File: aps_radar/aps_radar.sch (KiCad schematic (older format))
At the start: 0 parts

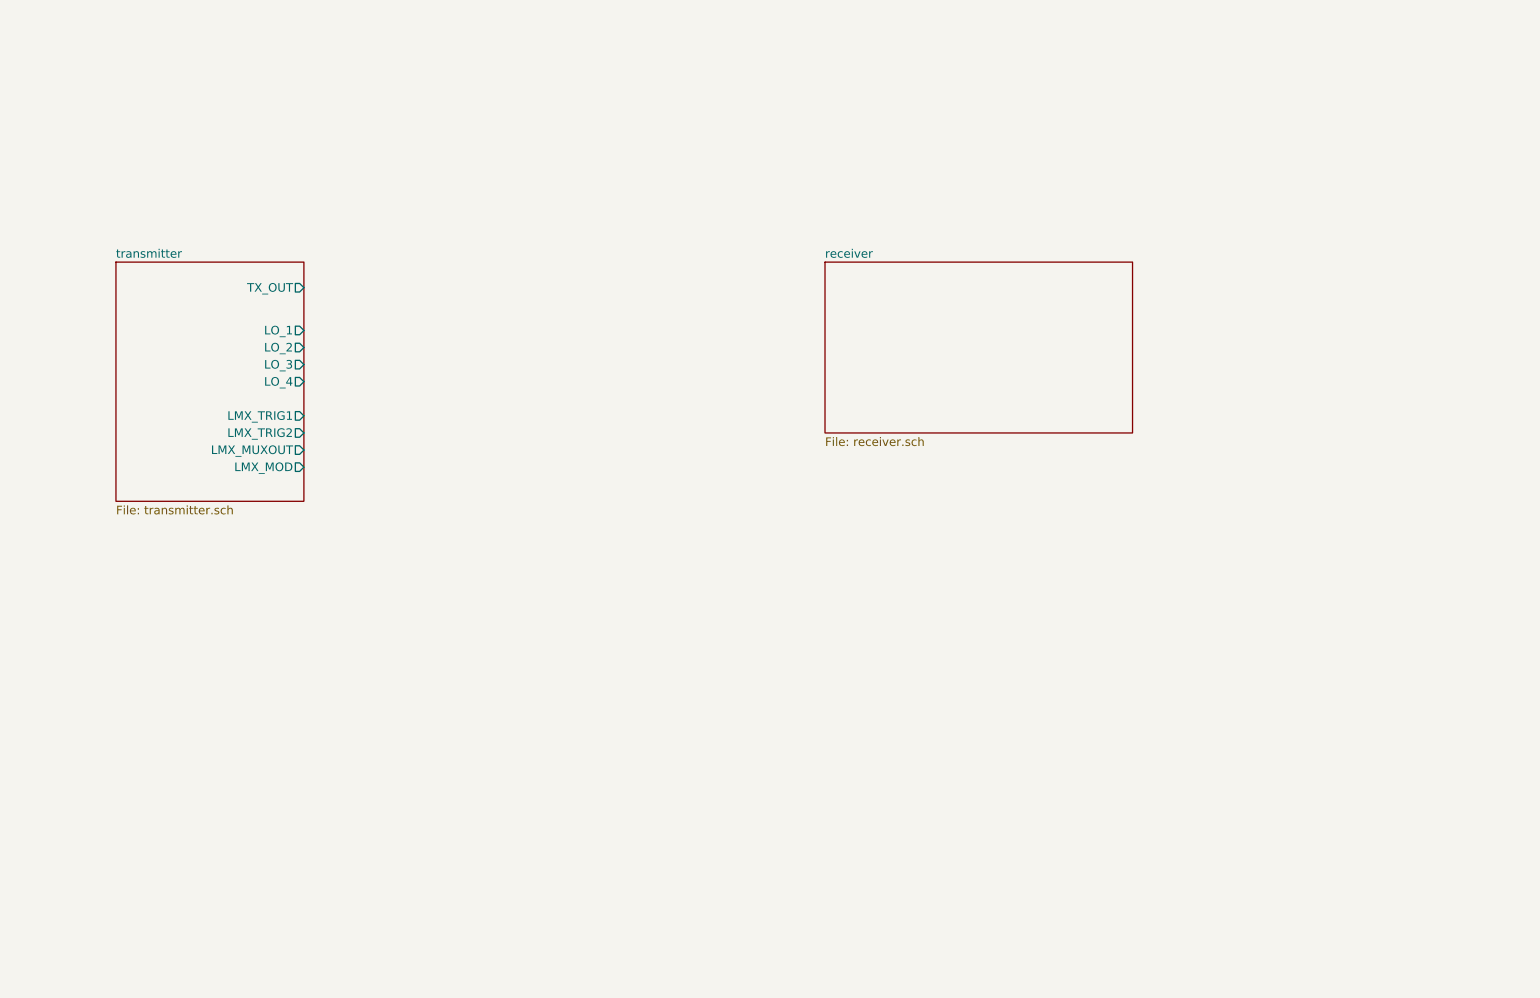
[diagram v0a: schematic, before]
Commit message: Integrated transmitter and receiver.  Need to add ferrite beads and power supply module.
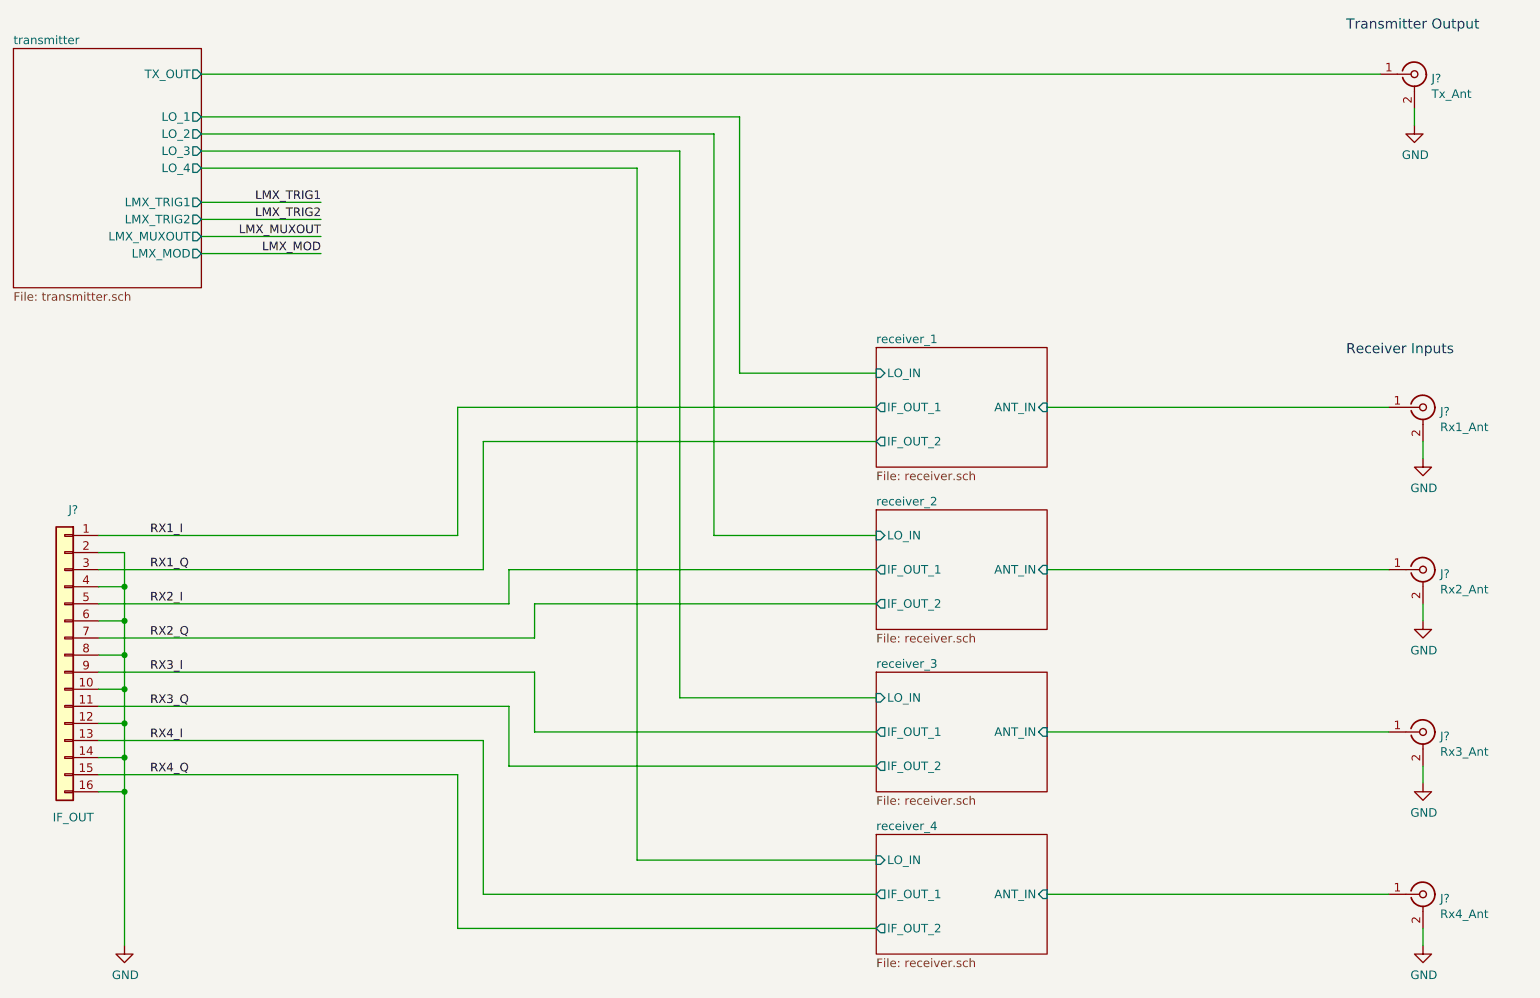
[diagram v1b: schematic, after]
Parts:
- added J?: Tx_Ant, symbol Connector:Conn_Coaxial
- added J?: Rx1_Ant, symbol Connector:Conn_Coaxial
- added J?: Rx2_Ant, symbol Connector:Conn_Coaxial
- added J?: Rx3_Ant, symbol Connector:Conn_Coaxial
- added J?: Rx4_Ant, symbol Connector:Conn_Coaxial
- added J?: IF_OUT, symbol Connector_Generic:Conn_01x16
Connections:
- net transmitter/TX_OUT: now also J?.1 (In)
- new net GND: J?.10 (Pin_10), J?.12 (Pin_12), J?.14 (Pin_14), J?.16 (Pin_16), J?.2 (Ext), J?.2 (Ext), J?.2 (Ext), J?.2 (Ext), J?.2 (Ext), J?.2 (Pin_2), J?.4 (Pin_4), J?.6 (Pin_6), J?.8 (Pin_8)
- new net RX1_I: J?.1 (Pin_1)
- new net RX1_Q: J?.3 (Pin_3)
- new net RX2_I: J?.5 (Pin_5)
- new net RX2_Q: J?.7 (Pin_7)
- new net RX3_I: J?.9 (Pin_9)
- new net RX3_Q: J?.11 (Pin_11)
- new net RX4_I: J?.13 (Pin_13)
- new net RX4_Q: J?.15 (Pin_15)
- new net receiver_1/ANT_IN: J?.1 (In)
- new net receiver_2/ANT_IN: J?.1 (In)
- new net receiver_3/ANT_IN: J?.1 (In)
- new net receiver_4/ANT_IN: J?.1 (In)
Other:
- note added: "Receiver Inputs"
- note added: "Transmitter Output"
